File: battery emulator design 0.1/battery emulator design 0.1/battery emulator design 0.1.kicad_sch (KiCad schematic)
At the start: 30 parts, among them J1 ExtPwrGnd, J10 ExtSetAll, J11 GND_CLIP, J12 V_Out1, J14 GND, J15 V_Out2, J16 V_Out3, J17 V_Out4, J6 ExtSet1, J7 ExtSet2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

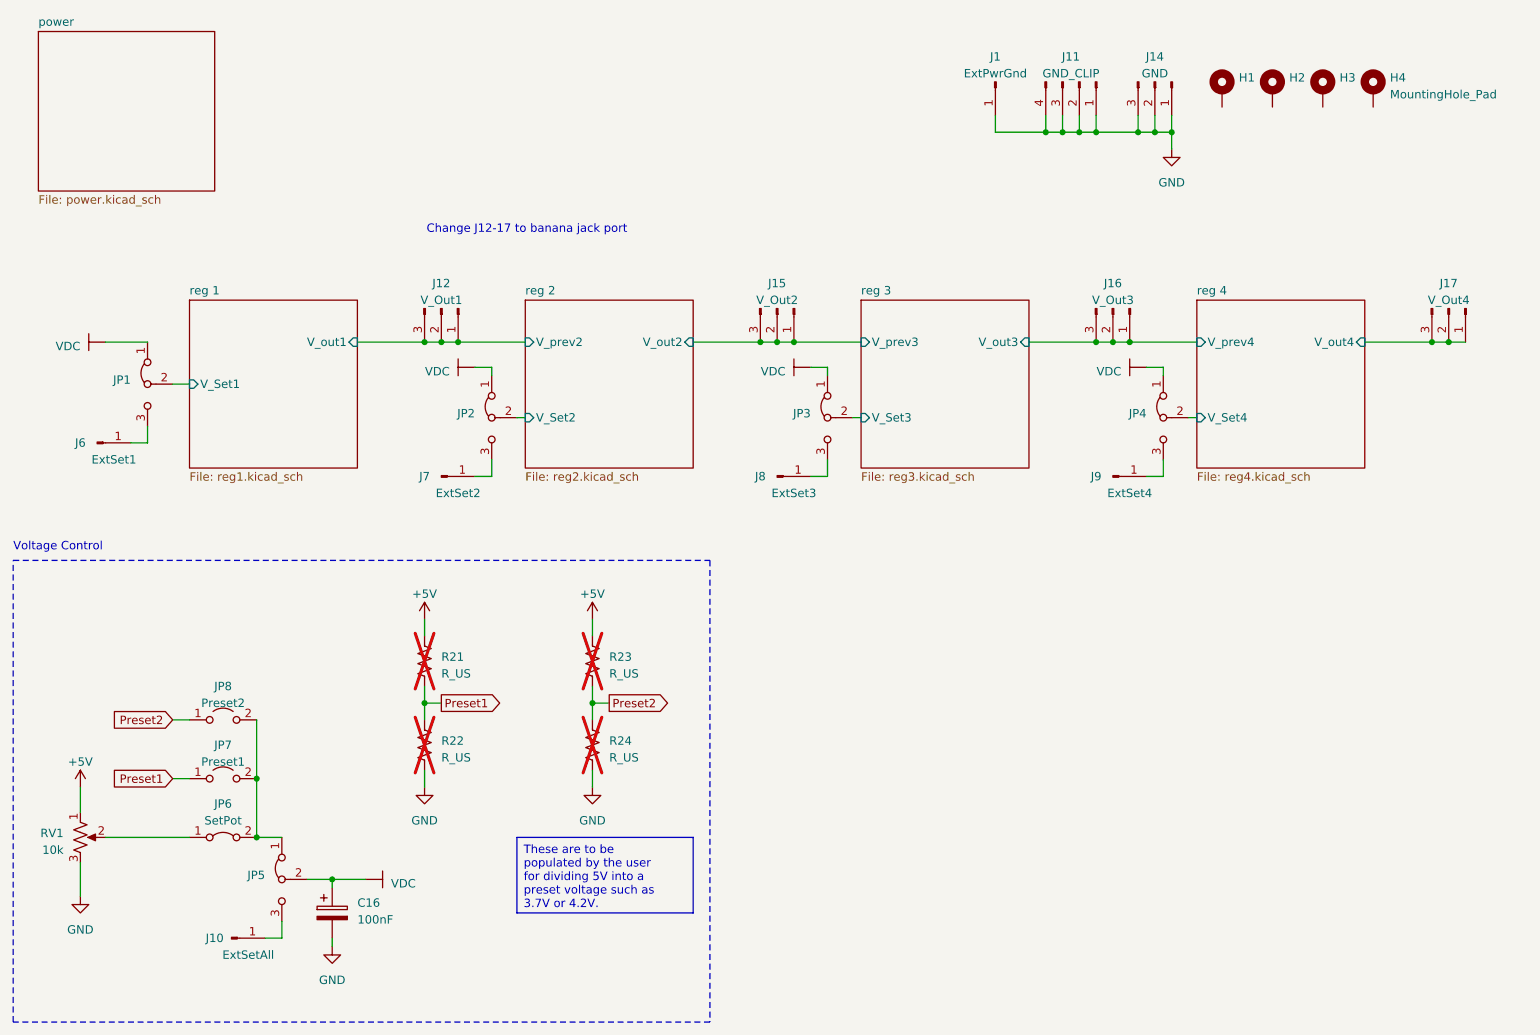
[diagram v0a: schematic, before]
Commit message: added pots to voltage buffers, other minor changes
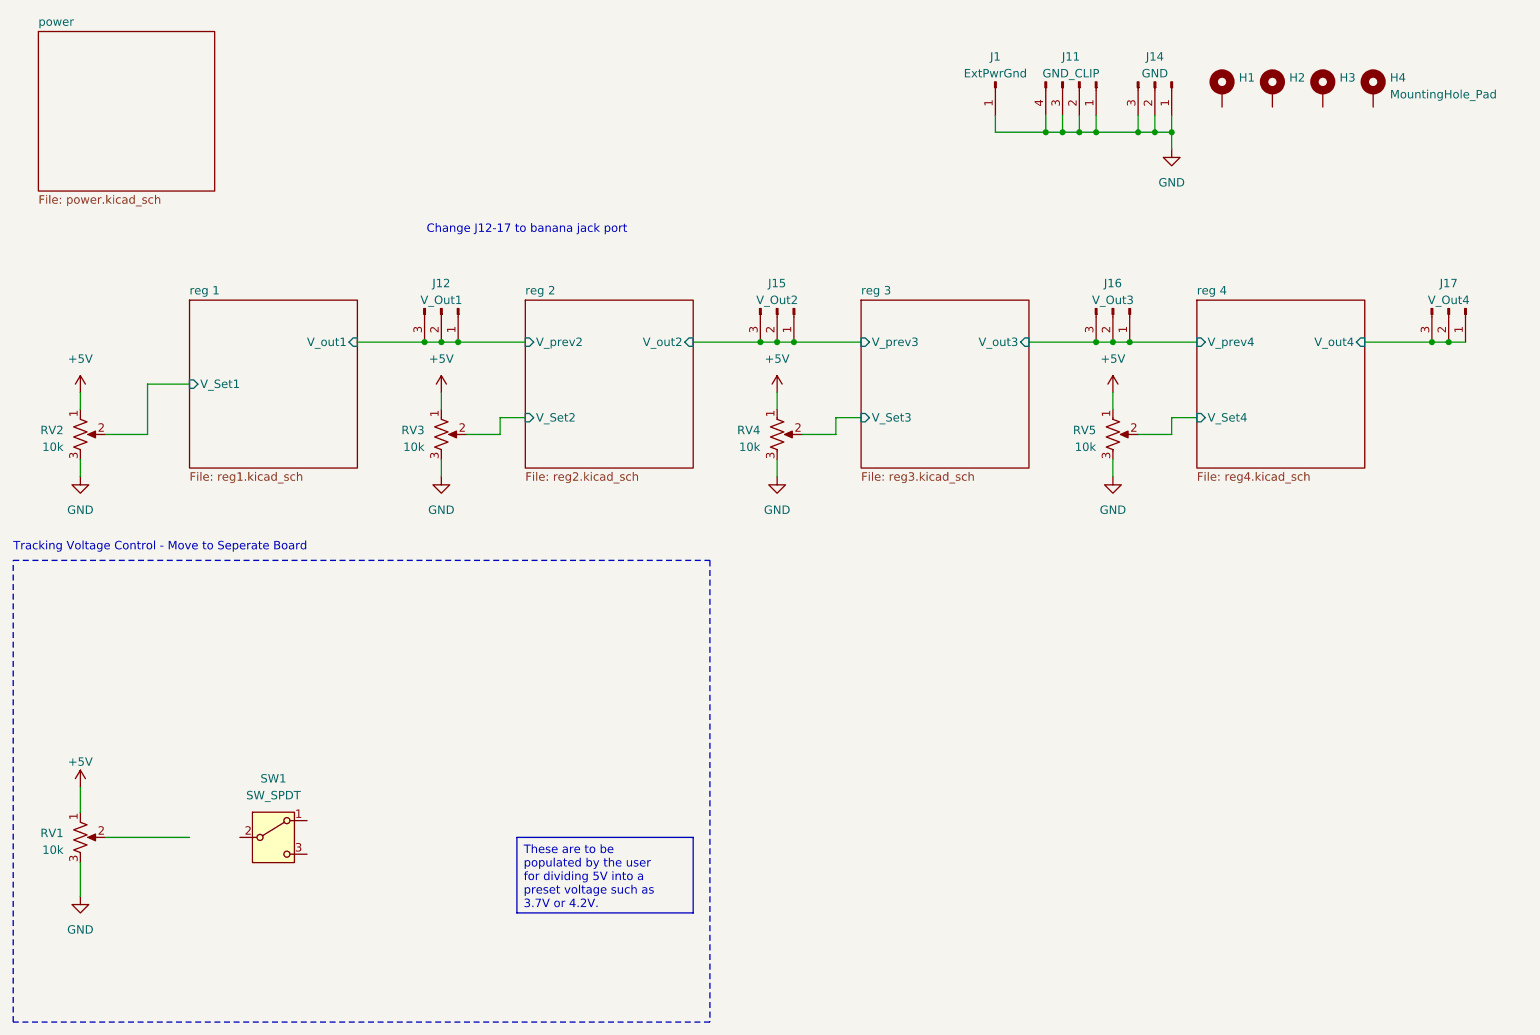
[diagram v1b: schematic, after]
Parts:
- removed C16: 100nF, Capacitor_THT:C_Disc_D3.4mm_W2.1mm_P2.50mm, symbol Device:C_Polarized
- removed J10: ExtSetAll, Connector_PinHeader_2.54mm:PinHeader_1x01_P2.54mm_Vertical, symbol Connector:Conn_01x01_Pin
- removed J6: ExtSet1, Connector_PinHeader_2.54mm:PinHeader_1x01_P2.54mm_Vertical, symbol Connector:Conn_01x01_Pin
- removed J7: ExtSet2, Connector_PinHeader_2.54mm:PinHeader_1x01_P2.54mm_Vertical, symbol Connector:Conn_01x01_Pin
- removed J8: ExtSet3, Connector_PinHeader_2.54mm:PinHeader_1x01_P2.54mm_Vertical, symbol Connector:Conn_01x01_Pin
- removed J9: ExtSet4, Connector_PinHeader_2.54mm:PinHeader_1x01_P2.54mm_Vertical, symbol Connector:Conn_01x01_Pin
- removed JP1, JP2, JP3, JP4, JP5: Jumper_3_Bridged12, Connector_PinHeader_2.54mm:PinHeader_1x03_P2.54mm_Vertical, symbol Jumper:Jumper_3_Bridged12
- removed JP6: SetPot, Connector_PinHeader_2.54mm:PinHeader_1x02_P2.54mm_Vertical, symbol Jumper:Jumper_2_Bridged
- removed JP7: Preset1, Connector_PinHeader_2.54mm:PinHeader_1x02_P2.54mm_Vertical, symbol Jumper:Jumper_2_Open
- removed JP8: Preset2, Connector_PinHeader_2.54mm:PinHeader_1x02_P2.54mm_Vertical, symbol Jumper:Jumper_2_Open
- removed R21, R22, R23, R24: R_US, Resistor_THT:R_Axial_DIN0207_L6.3mm_D2.5mm_P10.16mm_Horizontal, symbol Device:R_US
- added RV2, RV3, RV4, RV5: 10k, Potentiometer_THT:Potentiometer_Bourns_3386C_Horizontal, symbol Device:R_Potentiometer_US
- added SW1: SW_SPDT, symbol Switch:SW_SPDT
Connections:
- net +5V: now also RV2.1, RV3.1, RV4.1, RV5.1
- net GND: now also RV2.3, RV3.3, RV4.3, RV5.3
- net reg 1/V_Set1: now also RV2.2
- net reg 2/V_Set2: now also RV3.2
- net reg 3/V_Set3: now also RV4.2
- net reg 4/V_Set4: now also RV5.2
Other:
- note added: "Tracking Voltage Control - Move to Seperate Board"
- note removed: "Voltage Control"

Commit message: updating with all other boards
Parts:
- removed J1: ExtPwrGnd, Connector_PinHeader_2.54mm:PinHeader_1x01_P2.54mm_Vertical, symbol Connector:Conn_01x01_Pin
- removed J11: GND_CLIP, Connector_PinHeader_2.54mm:PinHeader_1x04_P2.54mm_Vertical, symbol Connector:Conn_01x04_Pin
- removed J14: GND, Connector_PinHeader_2.54mm:PinHeader_1x03_P2.54mm_Vertical, symbol Connector:Conn_01x03_Pin
- removed RV1: 10k, Potentiometer_THT:Potentiometer_Bourns_3386C_Horizontal, symbol Device:R_Potentiometer_US
- removed SW1: SW_SPDT, symbol Switch:SW_SPDT
- added J2: Conn_01x02_Pin, Connector_PinHeader_2.54mm:PinHeader_1x02_P2.54mm_Vertical, symbol Connector:Conn_01x02_Pin
- added R1, R22, R24, R4: 10k, Resistor_THT:R_Axial_DIN0207_L6.3mm_D2.5mm_P10.16mm_Horizontal, symbol Device:R_US
- added R2, R21, R23, R3: 3.3k, Resistor_THT:R_Axial_DIN0207_L6.3mm_D2.5mm_P10.16mm_Horizontal, symbol Device:R_US
- RV2, RV3, RV4, RV5: footprint Potentiometer_THT:Potentiometer_Bourns_3386C_Horizontal -> battery_emulator:PDB181
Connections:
- net +5V: now also R2.2, R21.2, R23.2, R3.2; no longer RV2.1, RV3.1, RV4.1, RV5.1
- net GND: now also R1.2, R22.2, R24.2, R4.2; no longer RV2.3, RV3.3, RV4.3, RV5.3
- net reg 1/V_Set1 renamed SurfBoard/S1A
- net reg 2/V_Set2 renamed SurfBoard/S2A
- net reg 3/V_Set3 renamed SurfBoard/S3A
- net reg 4/V_Set4 renamed SurfBoard/S4A
- new net: R3.1, RV3.1
- new net: R2.1, RV2.1
- new net: R21.1, RV4.1
- new net: R4.1, RV3.3
- new net: R22.1, RV4.3
- new net: R23.1, RV5.1
- new net: R24.1, RV5.3
- new net: R1.1, RV2.3
- new net SurfBoard/S1B: J2.1 (Pin_1)
- new net SurfBoard/SEL: J2.2 (Pin_2)
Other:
- added sheet SurfBoard (SurfBoard_sch.kicad_sch)
- note removed: "Change J12-17 to banana jack port"
- moved on the sheet: RV2, RV3, RV4, RV5
